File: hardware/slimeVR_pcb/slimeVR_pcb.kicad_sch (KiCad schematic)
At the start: 58 parts, among them J1 USB_C_Receptacle_USB2.0_16P, J3 Conn_ARM_JTAG_SWD_10, Q1 Q_Dual_NMOS_S1G1S2G2D2D2D1D1, SW1 SW_SPDT, SW3 SW_Push, U1 ESP32-S2-WROVER, U10 AP2112K-3.3, U2 TP4057, U3 ICM-45686, U5 QMC6309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

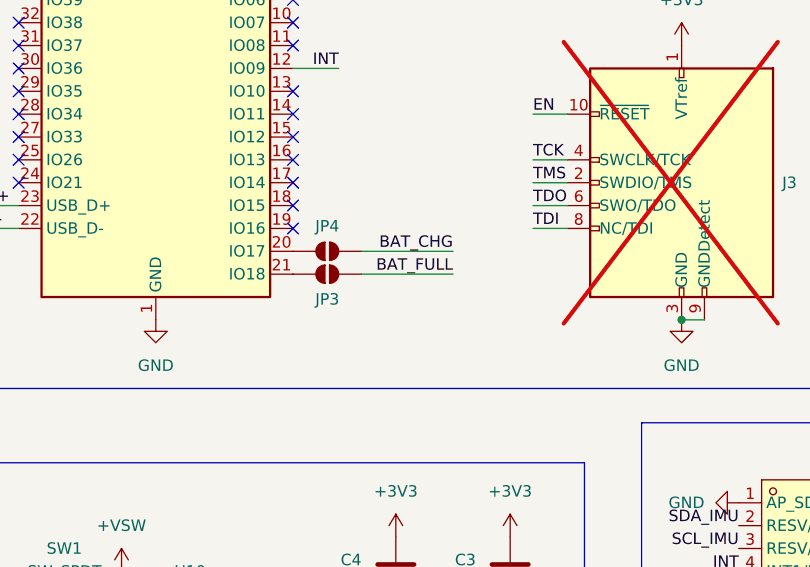
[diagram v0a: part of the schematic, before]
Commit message: replace charging signal jumpers with resistors these allow the internal ESD diodes of the ESP32S2 to clamp the valotage to safe levels
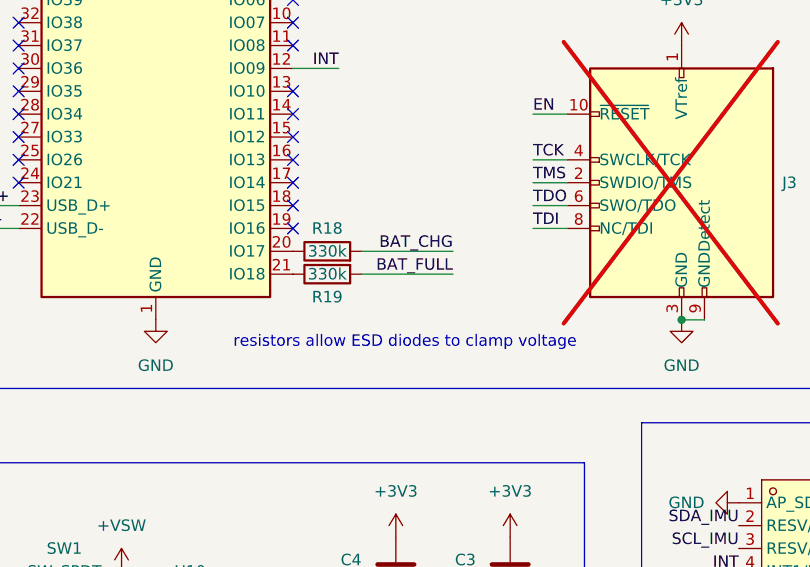
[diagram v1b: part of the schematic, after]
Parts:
- removed JP3, JP4: SolderJumper_2_Open, Jumper:SolderJumper-2_P1.3mm_Open_TrianglePad1.0x1.5mm, symbol Jumper:SolderJumper_2_Open
- added R18, R19: 330k, Resistor_SMD:R_0603_1608Metric_Pad0.98x0.95mm_HandSolder, symbol Device:R
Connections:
- net BAT_CHG: now also R18.2
- net BAT_FULL: now also R19.2
- net at U1.21 (IO18): now also R19.1
- net at U1.20 (IO17): now also R18.1
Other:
- note added: "resistors allow ESD diodes to clamp voltage"
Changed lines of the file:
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@@
 		)
 	)
+	(text "resistors allow ESD diodes to clamp voltage"
+		(exclude_from_sim no)
+		(at 136.906 87.63 0)
+		(effects
+			(font
+				(size 1.27 1.27)
+			)
+		)
+	)
 	(junction
 		(at 44.45 45.72)
@@
 	)
 	(symbol
-		(lib_id "Jumper:SolderJumper_2_Open")
-		(at 128.27 80.01 180)
-		(unit 1)
-		(exclude_from_sim no)
-		(in_bom no)
-		(on_board yes)
-		(dnp no)
-		(property "Reference" "JP3"
-			(at 128.27 82.804 0)
-			(effects
-				(font
-					(size 1.27 1.27)
-				)
-			)
-		)
-		(property "Value" "SolderJumper_2_Open"
-			(at 128.27 83.82 0)
-			(effects
-				(font
-					(size 1.27 1.27)
-				)
-				(hide yes)
-			)
-		)
-		(property "Footprint" "Jumper:SolderJumper-2_P1.3mm_Open_TrianglePad1.0x1.5mm"
-			(at 128.27 80.01 0)
-			(effects
-				(font
-					(size 1.27 1.27)
-				)
-				(hide yes)
-			)
-		)
-		(property "Datasheet" "~"
-			(at 128.27 80.01 0)
-			(effects
-				(font
-					(size 1.27 1.27)
-				)
-				(hide yes)
-			)
-		)
-		(property "Description" "Solder Jumper, 2-pole, open"
-			(at 128.27 80.01 0)
-			(effects
-				(font
-					(size 1.27 1.27)
-				)
-				(hide yes)
-			)
-		)
-		(pin "1"
-		)
-		(pin "2"
-		)
-		(instances
-			(project "slimeVR_pcb"
-				(path "/3cc72b9d-9220-40d8-b418-3d89bef5117e"
-					(reference "JP3")
-					(unit 1)
-				)
-			)
-		)
-	)
-	(symbol
 		(lib_id "Device:C")
 		(at 90.17 180.34 0)
@@
 	)
 	(symbol
-		(lib_id "Jumper:SolderJumper_2_Open")
-		(at 128.27 77.47 0)
-		(mirror y)
-		(unit 1)
-		(exclude_from_sim no)
-		(in_bom no)
-		(on_board yes)
-		(dnp no)
-		(property "Reference" "JP4"
-			(at 128.27 74.676 0)
-			(effects
-				(font
-					(size 1.27 1.27)
-				)
-			)
-		)
-		(property "Value" "SolderJumper_2_Open"
-			(at 128.27 73.66 0)
-			(effects
-				(font
-					(size 1.27 1.27)
-				)
-				(hide yes)
-			)
-		)
-		(property "Footprint" "Jumper:SolderJumper-2_P1.3mm_Open_TrianglePad1.0x1.5mm"
-			(at 128.27 77.47 0)
-			(effects
-				(font
-					(size 1.27 1.27)
-				)
-				(hide yes)
-			)
-		)
-		(property "Datasheet" "~"
-			(at 128.27 77.47 0)
-			(effects
-				(font
-					(size 1.27 1.27)
-				)
-				(hide yes)
-			)
-		)
-		(property "Description" "Solder Jumper, 2-pole, open"
-			(at 128.27 77.47 0)
-			(effects
-				(font
-					(size 1.27 1.27)
-				)
-				(hide yes)
-			)
-		)
-		(pin "1"
-		)
-		(pin "2"
-		)
-		(instances
-			(project "slimeVR_pcb"
-				(path "/3cc72b9d-9220-40d8-b418-3d89bef5117e"
-					(reference "JP4")
-					(unit 1)
-				)
-			)
-		)
-	)
-	(symbol
 		(lib_id "Device:C")
 		(at 148.59 113.03 0)
@@
 	)
 	(symbol
+		(lib_id "Device:R")
+		(at 128.27 80.01 90)
+		(mirror x)
+		(unit 1)
+		(exclude_from_sim no)
+		(in_bom yes)
+		(on_board yes)
+		(dnp no)
+		(property "Reference" "R19"
+			(at 128.27 82.55 90)
+			(effects
+				(font
+					(size 1.27 1.27)
+				)
+			)
+		)
+		(property "Value" "330k"
+			(at 128.27 80.01 90)
+			(effects
+				(font
+					(size 1.27 1.27)
+				)
+			)
+		)
+		(property "Footprint" "Resistor_SMD:R_0603_1608Metric_Pad0.98x0.95mm_HandSolder"
+			(at 128.27 78.232 90)
+			(effects
+				(font
+					(size 1.27 1.27)
+				)
+				(hide yes)
+			)
+		)
+		(property "Datasheet" "~"
+			(at 128.27 80.01 0)
+			(effects
+				(font
+					(size 1.27 1.27)
+				)
+				(hide yes)
+			)
+		)
+		(property "Description" "Resistor"
+			(at 128.27 80.01 0)
+			(effects
+				(font
+					(size 1.27 1.27)
+				)
+				(hide yes)
+			)
+		)
+		(pin "2"
+		)
+		(pin "1"
+		)
+		(instances
+			(project "slimeVR_pcb"
+				(path "/3cc72b9d-9220-40d8-b418-3d89bef5117e"
+					(reference "R19")
+					(unit 1)
+				)
+			)
+		)
+	)
+	(symbol
 		(lib_id "Connector:TestPoint")
 		(at 57.15 140.97 270)
@@
 					(unit 1)
 				)
+			)
+		)
+	)
+	(symbol
+		(lib_id "Device:R")
+		(at 128.27 77.47 90)
+		(unit 1)
+		(exclude_from_sim no)
+		(in_bom yes)
+		(on_board yes)
+		(dnp no)
+		(property "Reference" "R18"
+			(at 128.27 74.93 90)
+			(effects
+				(font
+					(size 1.27 1.27)
+				)
+			)
+		)
+		(property "Value" "330k"
+			(at 128.27 77.47 90)
+			(effects
+				(font
+					(size 1.27 1.27)
+				)
+			)
+		)
+		(property "Footprint" "Resistor_SMD:R_0603_1608Metric_Pad0.98x0.95mm_HandSolder"
+			(at 128.27 79.248 90)
+			(effects
+				(font
+					(size 1.27 1.27)
+				)
+				(hide yes)
+			)
+		)
+		(property "Datasheet" "~"
+			(at 128.27 77.47 0)
+			(effects
+				(font
+					(size 1.27 1.27)
+				)
+				(hide yes)
+			)
+		)
+		(property "Description" "Resistor"
+			(at 128.27 77.47 0)
+			(effects
+				(font
+					(size 1.27 1.27)
+				)
+				(hide yes)
+			)
+		)
+		(pin "2"
+		)
+		(pin "1"
+		)
+		(instances
+			(project "slimeVR_pcb"
+				(path "/3cc72b9d-9220-40d8-b418-3d89bef5117e"
+					(reference "R18")
+					(unit 1)
+				)

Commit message: cleanup, dw01 calc
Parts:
- renumbered SW3 to SW2
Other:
- note added: "V_OC = 140mV ... 180mv I_OC > 500mA <=> R_DS*2 < v_OC / I_OC R_DS < (140mV / 500mA) / 2 R_DS < 280mOhm"
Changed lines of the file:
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@@
 		)
 	)
+	(text "V_OC = 140mV ... 180mv\nI_OC > 500mA\n<=>\nR_DS*2 < v_OC / I_OC\nR_DS < (140mV / 500mA) / 2\nR_DS < 280mOhm"
+		(exclude_from_sim no)
+		(at 65.278 169.418 0)
+		(effects
+			(font
+				(size 1.27 1.27)
+			)
+			(justify left bottom)
+		)
+	)
 	(text "TODO: verify BAT_* never over 3.3V"
 		(exclude_from_sim no)
-		(at 114.808 164.338 0)
+		(at 115.062 191.008 0)
 		(effects
 			(font
@@
 		(on_board yes)
 		(dnp no)
-		(property "Reference" "SW3"
+		(property "Reference" "SW2"
 			(at 160.02 26.67 0)
 			(effects
@@
 			(project "slimeVR_pcb"
 				(path "/3cc72b9d-9220-40d8-b418-3d89bef5117e"
-					(reference "SW3")
+					(reference "SW2")
 					(unit 1)
 				)

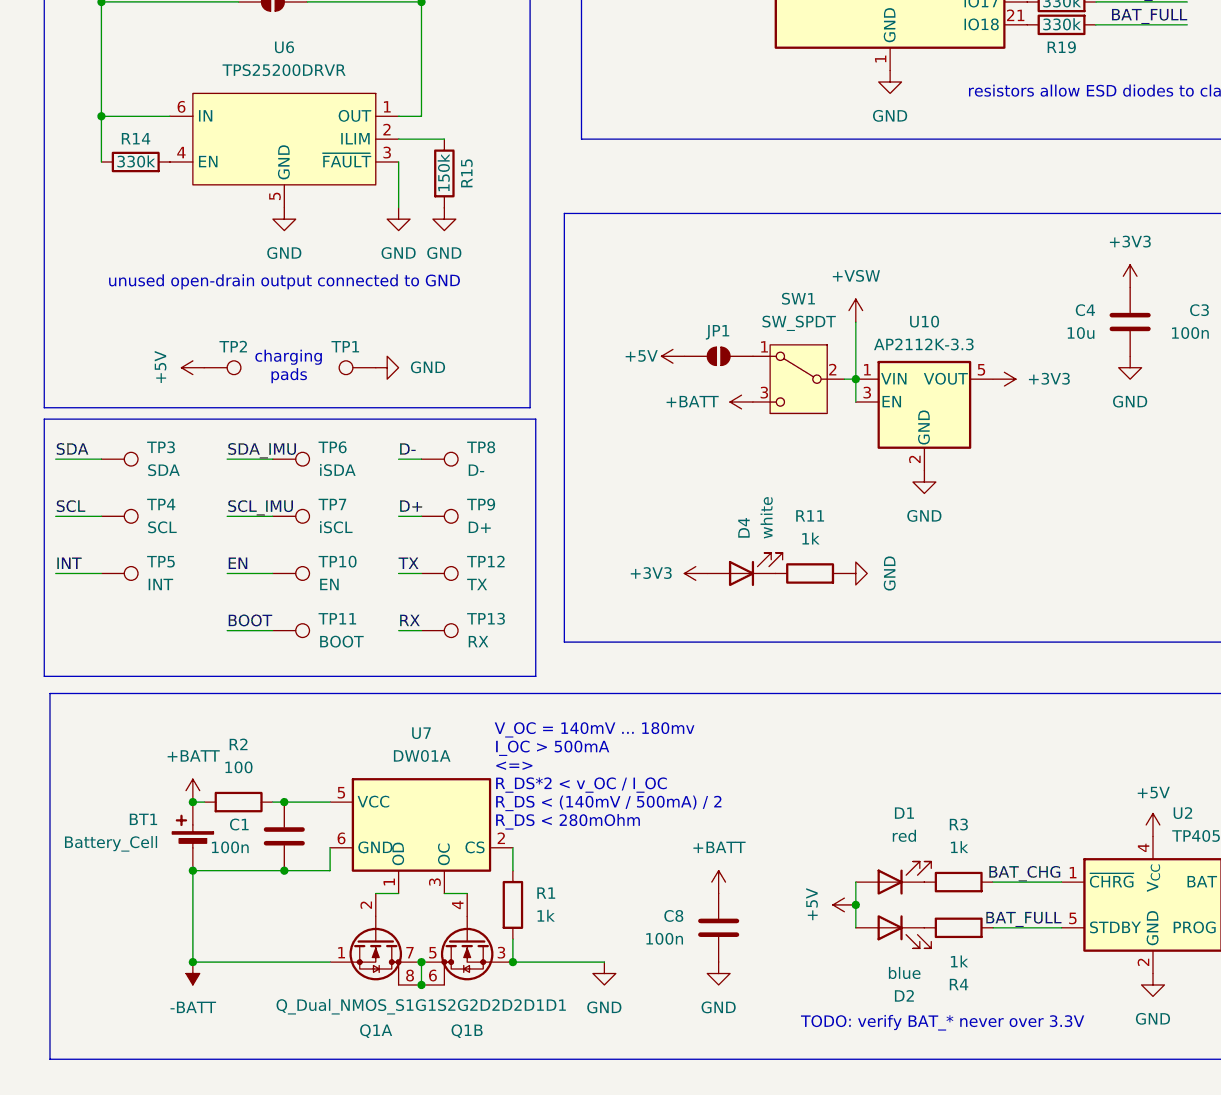
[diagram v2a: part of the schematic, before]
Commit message: add debugging footprints
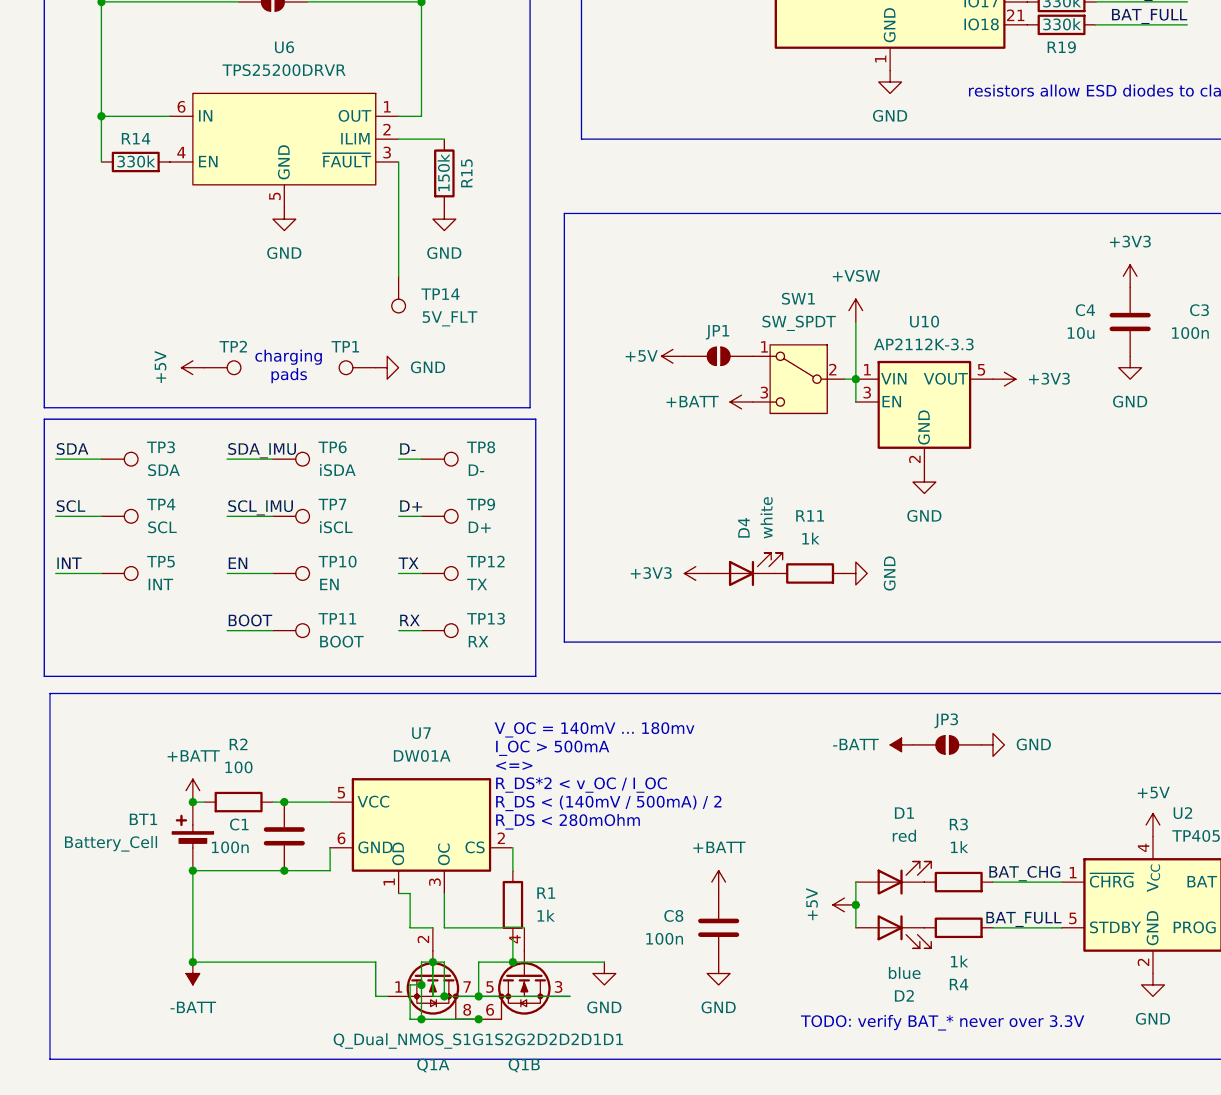
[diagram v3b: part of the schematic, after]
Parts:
- added JP3: SolderJumper_2_Open, Jumper:SolderJumper-2_P1.3mm_Open_TrianglePad1.0x1.5mm, symbol Jumper:SolderJumper_2_Open
- added TP14: 5V_FLT, TestPoint:TestPoint_Pad_D1.0mm, symbol Connector:TestPoint
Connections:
- net -BATT: now also JP3.2 (B)
- net GND: now also Q1.5 (D), Q1.6 (D), Q1.7 (D), Q1.8 (D), JP3.1 (A); no longer U6.3 (~{FAULT})
- new net: TP14.1, U6.3 (~{FAULT})
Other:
- note removed: "unused open-drain output connected to GND"
- moved on the sheet: Q1A, Q1B

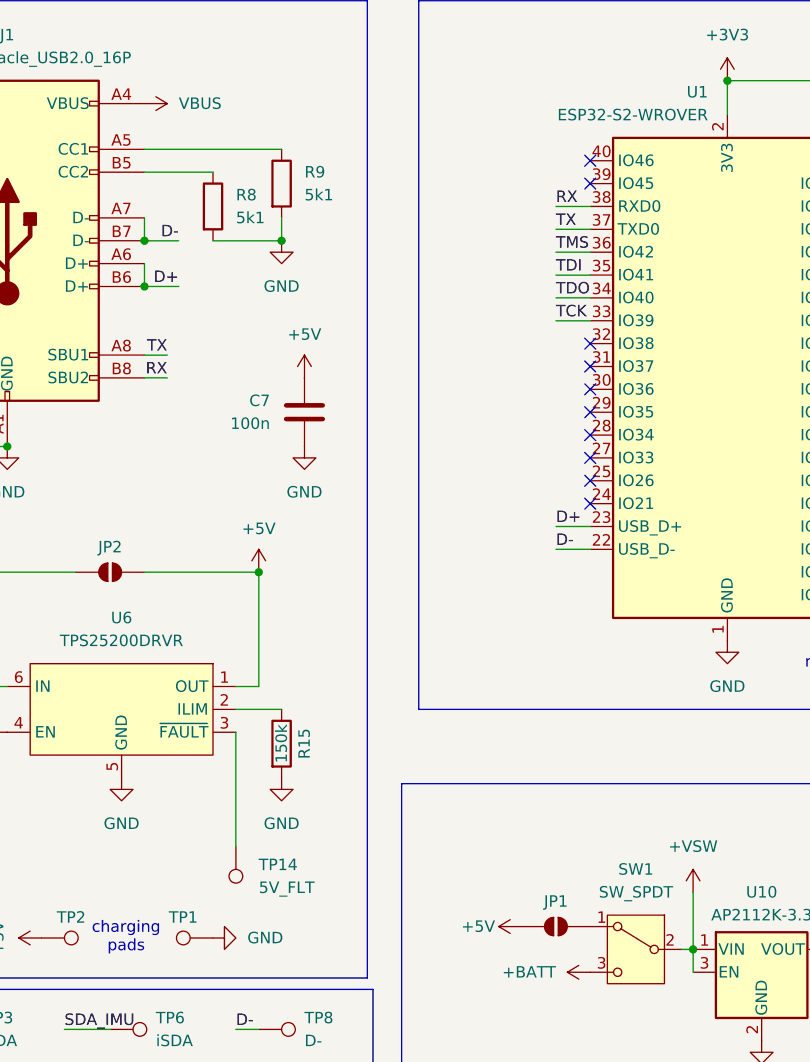
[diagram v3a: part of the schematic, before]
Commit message: allow reading vbus fault
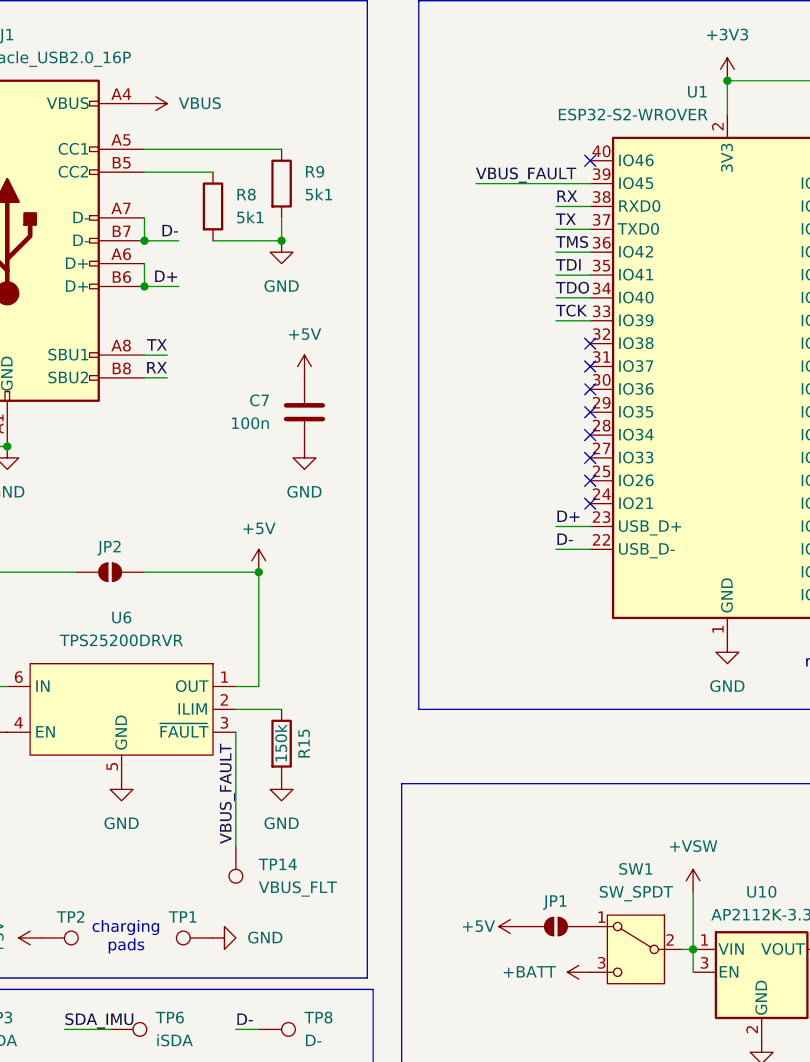
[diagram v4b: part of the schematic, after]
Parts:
- TP14: value 5V_FLT -> VBUS_FLT
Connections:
- net VBUS_FAULT: now reaches TP14.1, U6.3 (~{FAULT})
- net VBUS_FAULT: now also U1.39 (IO45)
- no-connect marks 25 -> 24
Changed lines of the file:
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@@
-	)
-	(no_connect
-		(at 93.98 34.29)
 	)
 	(no_connect
@@
 	(wire
 		(pts
+			(xy 81.28 34.29) (xy 93.98 34.29)
+		)
+		(stroke
+			(width 0)
+			(type default)
+		)
+	)
+	(wire
+		(pts
 			(xy 90.17 36.83) (xy 93.98 36.83)
 		)
@@
 		)
 	)
+	(label "VBUS_FAULT"
+		(at 54.61 96.52 270)
+		(effects
+			(font
+				(size 1.27 1.27)
+			)
+			(justify right bottom)
+		)
+	)
 	(label "SCL_IMU"
 		(at 35.56 134.62 0)
@@
 	(label "D-"
 		(at 54.61 128.27 0)
+		(effects
+			(font
+				(size 1.27 1.27)
+			)
+			(justify left bottom)
+		)
+	)
+	(label "VBUS_FAULT"
+		(at 81.28 34.29 0)
 		(effects
 			(font
@@
 			)
 		)
-		(property "Value" "5V_FLT"
+		(property "Value" "VBUS_FLT"
 			(at 57.15 112.5219 0)
 			(effects

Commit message: partsel round 1
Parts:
- BT1: value Battery_Cell -> 804040 Li-Po; now left out of the parts list
- C1, C2, C3, C7, C8: LCSC (none) -> C14663
- C4: LCSC (none) -> C19702
- C6: LCSC (none) -> C15849
- J1: value USB_C_Receptacle_USB2.0_16P -> HRO_TYPE-C-31-M-12; LCSC (none) -> C165948; LCSC Part (none) -> C165948
- R1, R10, R11, R3, R4, R6, R7: LCSC (none) -> C21190
- R12, R13, R16, R17: LCSC (none) -> C23162
- R14, R18, R19: LCSC (none) -> C23024
- R15: LCSC (none) -> C22807
- R2: LCSC (none) -> C22775
- R5: LCSC (none) -> C4177
- R8, R9: LCSC (none) -> C23186
- SW1: value SW_SPDT -> SK12D07VG4; LCSC (none) -> C393937; LCSC Part (none) -> C393937
- U10: LCSC (none) -> C51118; LCSC Part (none) -> C51118
- U2: LCSC (none) -> C725791; LCSC Part (none) -> C725791
- U3: LCSC (none) -> C22459454
- U5: LCSC (none) -> C5439871
- U6: LCSC (none) -> C128401
- U7: LCSC (none) -> C2927799; LCSC Part (none) -> C2927799
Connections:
- net GND: no longer Q1.5 (D), Q1.6 (D), Q1.7 (D), Q1.8 (D)
- new net: Q1.5 (D), Q1.6 (D), Q1.7 (D), Q1.8 (D)
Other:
- moved on the sheet: Q1A, Q1B

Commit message: partsel round 2
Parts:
- removed Q1: Q_Dual_NMOS_S1G1S2G2D2D2D1D1, Package_TO_SOT_SMD:SOT-23-8_Handsoldering, symbol Transistor_FET:Q_Dual_NMOS_S1G1S2G2D2D2D1D1
- added Q1: 8205A, Package_TO_SOT_SMD:SOT-23-6, symbol slime_parts:8205A
- D1: LCSC (none) -> C2286; LCSC Part (none) -> C2286
- D2: LCSC (none) -> C2288; LCSC Part (none) -> C2288
- D3: LCSC (none) -> C2289; LCSC Part (none) -> C2289
- D4: LCSC (none) -> C2290; LCSC Part (none) -> C2290
- R14, R18, R19: value 330k -> 300k
- TP10, TP11, TP12, TP13, TP14, TP3, TP4, TP5, TP6, TP7, TP8, TP9: now left out of the parts list
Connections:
- net -BATT: now also Q1.1 (S1)
- net GND: now also Q1.3 (S2)
- net at U7.1 (OD): now also Q1.6 (G1)
- net at U7.3 (OC): now also Q1.4 (G2)
- net VBUS_FAULT renamed VBUS_FLT
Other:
- moved on the sheet: TP14
